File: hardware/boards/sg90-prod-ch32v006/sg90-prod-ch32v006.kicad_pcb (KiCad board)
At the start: 6 copper layers, 12.5 x 10 mm, 36 parts, among them J1 Servo Input, J2 Motor, J3 Debug, J4 Potentiometer, Q1 AO3401A, U1 TPAP2210K-3.3TRG1, U2 SN74LVC1G07DRLR_C19829624, U3 DRV8837DSGR-JSM, U4 CH32V006F8U6

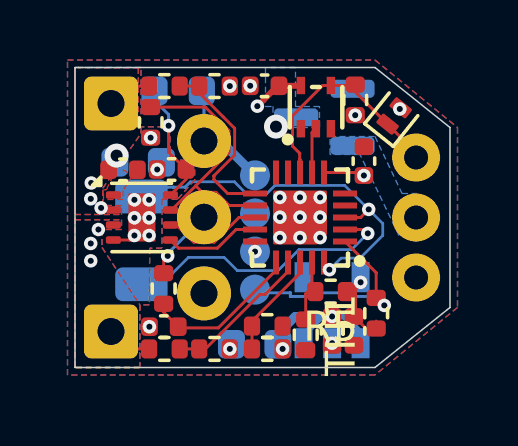
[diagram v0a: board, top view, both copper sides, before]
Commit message: make sg90-pprod-ch32v006 board DATA line 5v tolerant
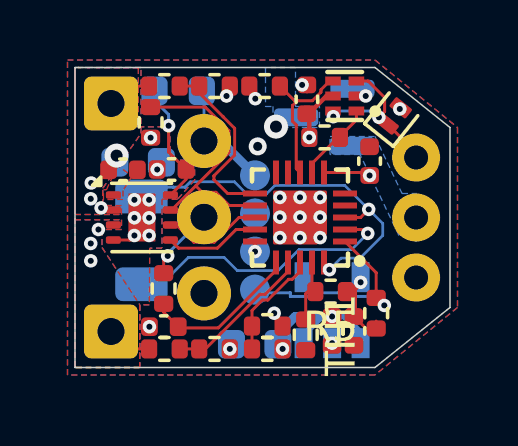
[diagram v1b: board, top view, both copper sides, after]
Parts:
- removed NT1: NetTie_2, shared:NetTie-2_SMD_0.2mm
- added R13: 47kΩ, Resistor_SMD:R_0402_1005Metric, F.Cu at (108.3, 92.3)
- D1: value PESD5V0L1UL -> ESD
- R1: value 1kΩ -> 10kΩ
- U2: value SN74LVC1G07DRLR_C19829624 -> SN74LVC2G07DRYR(UMW); footprint shared:SOT-553-5_L1.6-W1.2-P0.50-LS1.6-BL -> shared:SON-6_L1.5-W1.0-P0.50-BL
- moved R1 3.05 mm to (106.3, 90.6), turned to 0 degrees
- moved C4 1.48 mm to (107.7, 91.1), turned to 90 degrees
- moved U2 1.03 mm to (109.0, 91.0), turned to 90 degrees
- moved C9 0.19 mm to (109.8, 93.1)
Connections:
- R1 pad 2: /DATA -> /RX
- U2 pad 1: unconnected-(U2-NC-Pad1) -> /TX
- U2 pad 2: /TX -> GND
- U2 pad 3: GND -> /DATA
- U2 pad 4: /DATA -> /RX
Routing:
- net /RX: track 0.44 -> 4.85 mm
- net /DATA: track 7.19 -> 5.10 mm, vias 0 -> 2
- net /TX: track 1.51 -> 2.70 mm
- net GND: track 0.00 -> 0.25 mm, vias 15 -> 18

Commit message: echo-free data line with RX disable latch
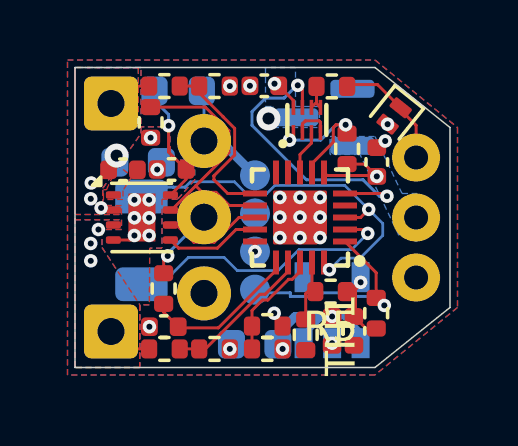
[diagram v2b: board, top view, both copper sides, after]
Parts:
- R1: value 10kΩ -> 47kΩ
- R13: value 47kΩ -> 68Ω
- U2: value SN74LVC2G07DRYR(UMW) -> 74LVC2G125; footprint shared:SON-6_L1.5-W1.0-P0.50-BL -> shared:X2-DFN1210-8_L1.2-W1.0-P0.30-BL
- moved R1 3.45 mm to (109.1, 92.7), turned to -90 degrees
- moved R13 1.72 mm to (108.6, 90.6), turned to 0 degrees
- moved U2 1.49 mm to (107.7, 91.8), turned to 0 degrees
- moved C4 1.49 mm to (106.3, 90.6), turned to 180 degrees
- moved C9 0.24 mm to (110.1, 93.2)
- turned D1 to -128.659 degrees
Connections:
- R1 pad 1: +3.3V -> /TX
- R1 pad 2: /RX -> +3.3V
- R13 pad 1: /TX -> /BUF
- R13 pad 2: +3.3V -> /DATA
- U2 pad 3: /DATA -> /RX
- U2 pad 4: /RX -> GND
- U2 pad 5: +3.3V -> /BUF
- U2 pad 6: /DATA -> /BUF
- U4 pad 5: unconnected-(U4-PD0/T1/TX_/SDA_/OPN1-Pad5) -> /DE
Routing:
- net /DE: track 0.00 -> 10.1 mm, vias 0 -> 2
- net /RX: track 4.85 -> 1.49 mm
- net /BUF: track 0.00 -> 1.52 mm
- net /TX: track 2.70 -> 4.02 mm, vias 0 -> 2
- net /DATA: track 5.10 -> 3.95 mm, vias 2 -> 0
- net GND: track 0.25 -> 1.30 mm, vias 18 -> 17
- net /OUTB: track 1.51 -> 0.69 mm
- net /OUTA: track 1.51 -> 0.69 mm
- net /VSYS: track 5.45 -> 4.77 mm
- net +3.3V: track 9.87 -> 9.31 mm, vias 4 -> 3
- net /VSNB: track 4.98 -> 4.47 mm

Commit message: Normalize line endings to LF
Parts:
- removed NT3: NetTie_2, shared:NetTie-2_SMD_0.2mm
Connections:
- net /ISNS+ renamed /ISNS
- U4 pad 2: /ISNS- -> unconnected-(U4-PA1/T1/T2/OPN0/XI/A1-Pad2)
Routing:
- net /ISNS-: track 8.24 -> 0.00 mm, vias 1 -> 0
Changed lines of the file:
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@@
 	(net 8 "/OUTA")
 	(net 9 "/RX")
-	(net 10 "/ISNS+")
+	(net 10 "/ISNS")
 	(net 11 "/TX")
 	(net 12 "/DATA")
@@
 	(net 17 "/EN")
 	(net 18 "/VSNA")
-	(net 19 "/ISNS-")
+	(net 19 "unconnected-(U4-PA1{slash}T1{slash}T2{slash}OPN0{slash}XI{slash}A1-Pad2)")
 	(net 20 "+3.3V")
 	(net 21 "/VNTC")
@@
 			(size 0.2 0.8)
 			(layers "F.Cu" "F.Mask" "F.Paste")
-			(net 19 "/ISNS-")
+			(net 19 "unconnected-(U4-PA1{slash}T1{slash}T2{slash}OPN0{slash}XI{slash}A1-Pad2)")
 			(pinfunction "PA1/T1/T2/OPN0/XI/A1")
-			(pintype "bidirectional")
+			(pintype "bidirectional+no_connect")
 		)
 		(pad "3" smd rect
@@
 			(size 0.2 0.8)
 			(layers "F.Cu" "F.Mask" "F.Paste")
-			(net 10 "/ISNS+")
+			(net 10 "/ISNS")
 			(pinfunction "PA2/T1/T2/U2TX_/OPP0/XO/A0")
 			(pintype "bidirectional")
@@
 			(size 0.2 0.8)
 			(layers "F.Cu" "F.Mask" "F.Paste")
-			(net 10 "/ISNS+")
+			(net 10 "/ISNS")
 			(pinfunction "PD6/T2/RX/TX_/MOSI_/A6")
 			(pintype "bidirectional")
@@
 			(size 0.1 0.1)
 			(layers "B.Cu")
-			(net 10 "/ISNS+")
+			(net 10 "/ISNS")
 			(pinfunction "1")
 			(pintype "passive")
@@
 		)
 	)
-	(footprint "shared:NetTie-2_SMD_0.2mm"
-		(layer "B.Cu")
-		(at 103.15 96.86 180)
-		(descr "Net tie, 2 pin, 0.2mm trace width for fine pitch boards")
-		(tags "net tie")
-		(property "Reference" "NT3"
-			(at 0 0.7 0)
-			(layer "B.SilkS")
-			(hide yes)
-			(effects
-				(font
-					(size 0.5 0.5)
-					(thickness 0.1)
-				)
-				(justify mirror)
-			)
-		)
-		(property "Value" "NetTie_2"
-			(at 0 -0.7 0)
-			(layer "B.Fab")
-			(hide yes)
-			(effects
-				(font
-					(size 0.5 0.5)
-					(thickness 0.1)
-				)
-				(justify mirror)
-			)
-		)
-		(property "Datasheet" "~"
-			(at 0 0 0)
-			(layer "B.Fab")
-			(hide yes)
-			(effects
-				(font
-					(size 1.27 1.27)
-					(thickness 0.15)
-				)
-				(justify mirror)
-			)
-		)
-		(property "Description" "Net tie, 2 pins"
-			(at 0 0 0)
-			(layer "B.Fab")
-			(hide yes)
-			(effects
-				(font
-					(size 1.27 1.27)
-					(thickness 0.15)
-				)
-				(justify mirror)
-			)
-		)
-		(property ki_fp_filters "Net*Tie*")
-		(sheetname "/")
-		(sheetfile "sg90-prod-ch32v006.kicad_sch")
-		(attr exclude_from_pos_files exclude_from_bom allow_soldermask_bridges)
-		(net_tie_pad_groups "1,2")
-		(fp_line
-			(start 0.1 0)
-			(end -0.1 0)
-			(stroke
-				(width 0.1)
-				(type solid)
-			)
-			(layer "B.Cu")
-		)
-		(pad "1" smd circle
-			(at -0.1 0 180)
-			(size 0.1 0.1)
-			(layers "B.Cu")
-			(net 19 "/ISNS-")
-			(pinfunction "1")
-			(pintype "passive")
-			(clearance 0.1)
-		)
-		(pad "2" smd circle
-			(at 0.1 0 180)
-			(size 0.1 0.1)
-			(layers "B.Cu")
-			(net 1 "GND")
-			(pinfunction "2")
-			(pintype "passive")
-			(clearance 0.1)
-		)
-		(embedded_fonts no)
-	)
 	(footprint "Capacitor_SMD:C_0603_1608Metric"
 		(layer "B.Cu")
@@
 	)
 	(segment
-		(start 109.63 95.4)
-		(end 109.76 95.53)
-		(width 0.1)
-		(layer "F.Cu")
-		(net 19)
-	)
-	(segment
-		(start 109 95.4)
-		(end 109.63 95.4)
-		(width 0.1)
-		(layer "F.Cu")
-		(net 19)
-	)
-	(via
-		(at 109.76 95.53)
-		(size 0.45)
-		(drill 0.2)
-		(layers "F.Cu" "B.Cu")
-		(free yes)
-		(net 19)
-	)
-	(segment
-		(start 103.78 96.33)
-		(end 104.97 96.33)
-		(width 0.09)
-		(layer "B.Cu")
-		(net 19)
-	)
-	(segment
-		(start 104.97 96.33)
-		(end 105.41 96.77)
-		(width 0.09)
-		(layer "B.Cu")
-		(net 19)
-	)
-	(segment
-		(start 107.468 96.07)
-		(end 109.22 96.07)
-		(width 0.09)
-		(layer "B.Cu")
-		(net 19)
-	)
-	(segment
-		(start 103.25 96.86)
-		(end 103.78 96.33)
-		(width 0.09)
-		(layer "B.Cu")
-		(net 19)
-	)
-	(segment
-		(start 106.768 96.77)
-		(end 107.468 96.07)
-		(width 0.09)
-		(layer "B.Cu")
-		(net 19)
-	)
-	(segment
-		(start 109.22 96.07)
-		(end 109.76 95.53)
-		(width 0.09)
-		(layer "B.Cu")
-		(net 19)
-	)
-	(segment
-		(start 105.41 96.77)
-		(end 106.768 96.77)
-		(width 0.09)
-		(layer "B.Cu")
-		(net 19)
-	)
-	(segment

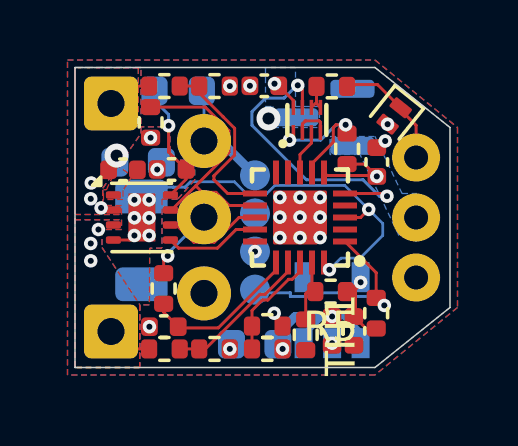
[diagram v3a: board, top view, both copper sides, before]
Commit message: add 0.1uF cap between motor terminals to reduce EMI
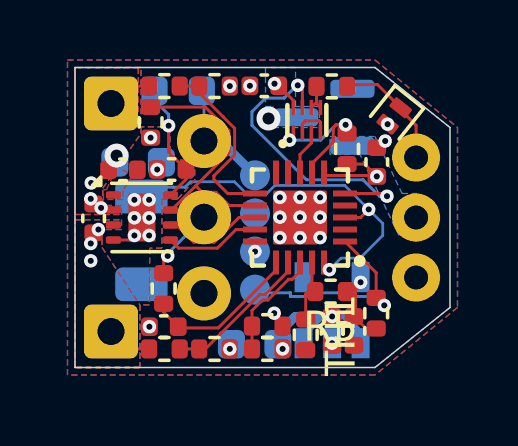
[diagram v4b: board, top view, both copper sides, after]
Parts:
- added C14: 0.1µF, Capacitor_SMD:C_0402_1005Metric, F.Cu at (100.6, 95.0)

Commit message: update sg90-prod-ch32v006
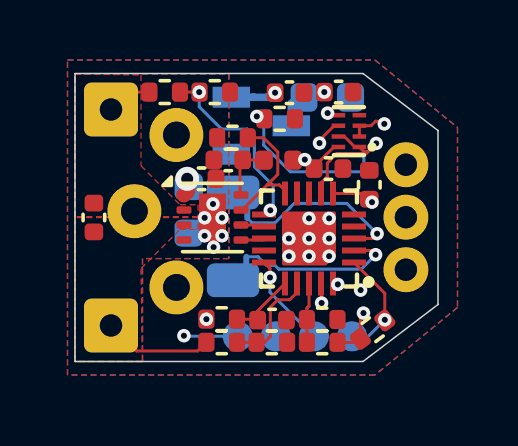
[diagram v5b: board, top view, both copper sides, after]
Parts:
- removed C14, C5: 0.1µF, Capacitor_SMD:C_0402_1005Metric
- removed D1: ESD, Diode_SMD:D_SOD-882
- removed Q1: AO3401A, Package_TO_SOT_SMD:SOT-23
- removed R10, R12: 10kΩ, Resistor_SMD:R_0402_1005Metric
- removed R11: 20kΩ, Resistor_SMD:R_0402_1005Metric
- removed R13: 68Ω, Resistor_SMD:R_0402_1005Metric
- removed U2: 74LVC2G125, shared:X2-DFN1210-8_L1.2-W1.0-P0.30-BL
- removed U3: DRV8837DSGR-JSM, Package_SON:WSON-8-1EP_2x2mm_P0.5mm_EP0.9x1.6mm
- added C10: 10µF, Capacitor_SMD:C_0603_1608Metric, B.Cu at (103.8, 94.7)
- added C11: 0.1µF, Capacitor_SMD:C_0402_1005Metric, F.Cu at (109.8, 93.9)
- added NT1: NetTie_2, shared:NetTie-2_SMD_0.2mm, B.Cu at (105.7, 94.8)
- added RS1: 0.1Ω 1%, Resistor_SMD:R_1206_3216Metric, B.Cu at (105.3, 95.6)
- added U5: CH32V006F8U6, shared:UQFN-20_L3.0-W3.0-P0.40-BL-EP1.7, F.Cu at (107.8, 95.7)
- added U6: 74LVC2G241GS,115, shared:XSON-8_L1.4-W1.0-P0.35-S0.55-BL, F.Cu at (109.1, 92.1)
- C3: value 1µF -> 10µF
- C8: value 10µF -> 0.1µF; footprint Capacitor_SMD:C_0603_1608Metric -> Capacitor_SMD:C_0402_1005Metric; moved to F.Cu
- FB1: footprint Inductor_SMD:L_0603_1608Metric -> Inductor_SMD:L_0402_1005Metric; moved to F.Cu
- R1: value 47kΩ -> 10kΩ
- R4: value 0.1Ω 1% -> 10kΩ; footprint Resistor_SMD:R_1206_3216Metric -> Resistor_SMD:R_0402_1005Metric; moved to F.Cu
- R5: value 10kΩ -> 20kΩ
- R9: value 20kΩ -> 10kΩ
- U1: value TPAP2210K-3.3TRG1 -> H7133-1; footprint shared:SOT-23-5_L2.9-W1.6-P0.95-LS2.8-BR -> shared:SOT-23-3_L2.9-W1.3-P1.90-LS2.4-BR
- U4: value CH32V006F8U6 -> DRV8837; footprint shared:UQFN-20_L3.0-W3.0-P0.40-BL-EP1.7 -> Package_SON:WSON-8-1EP_2x2mm_P0.5mm_EP0.9x1.6mm
- moved R9 10.0 mm to (108.2, 99.2), turned to 180 degrees
- moved R6 9.12 mm to (104.7, 90.8), turned to 0 degrees
- moved R5 8.65 mm to (103.0, 90.8), turned to 0 degrees
- moved C1 8.57 mm to (108.4, 91.0), turned to 0 degrees
- moved R4 8.26 mm to (109.9, 98.7), turned to 37.2 degrees
- moved C3 8.23 mm to (107.2, 90.8), turned to 0 degrees
- moved C2 7.96 mm to (108.8, 90.8), turned to 0 degrees
- moved U1 6.59 mm to (106.2, 91.9), turned to 180 degrees
- moved C6 6.04 mm to (106.6, 98.4), turned to 0 degrees
- moved C9 5.87 mm to (104.2, 93.7), turned to 0 degrees
- moved FB1 4.07 mm to (106.8, 93.1)
- moved J3 3.71 mm to (107.3, 99.0), turned to 0 degrees
- moved NT2 3.58 mm to (105.7, 96.5), turned to -90 degrees
- moved C7 3.53 mm to (105.1, 93.1), turned to 180 degrees
- moved C4 3.49 mm to (108.5, 93.4), turned to 0 degrees
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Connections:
- C1 pad 1: /VSYS -> VSYS
- C2 pad 1: /VSYS -> VSYS
- C3 pad 1: +3.3V -> +3V3
- C4 pad 1: +3.3V -> +3V3
- C6 pad 1: /3V3_DRV -> /VPOS
- C6 pad 2: PGND -> GND
- C7 pad 1: /VSYS -> /3V3_DRV
- C8 pad 1: /VSYS -> /MOT_A
- C8 pad 2: PGND -> /MOT_B
- C9 pad 1: +3.3V -> VSYS
- C9 pad 2: GND -> PGND
- FB1 pad 1: +3.3V -> +3V3
- J1 pad 1: GND -> VSYS
- J1 pad 2: VIN -> GND
- J2 pad 1: /OUTA -> /MOT_A
- J2 pad 2: /OUTB -> /MOT_B
- J3 pad 1: +3.3V -> +3V3
- J4 pad 1: +3.3V -> +3V3
- NT2 pad 1: /ISNS -> /ISNS-
- NT2 pad 2: PGND -> GND
- R1 pad 1: /TX -> GND
- R1 pad 2: +3.3V -> /TX_EN
- R4 pad 1: GND -> +3V3
- R4 pad 2: PGND -> /nRST
- R5 pad 1: +3.3V -> /MOT_A
- R5 pad 2: /VNTC -> /VSNA
- R6 pad 1: +3.3V -> /VSNA
- R6 pad 2: /nRST -> GND
- R7 pad 1: /VSYS -> /MOT_B
- R7 pad 2: /VINS -> /VSNB
- R8 pad 1: /VINS -> /VSNB
- R9 pad 1: /OUTA -> +3V3
- R9 pad 2: /VSNA -> /VNTC
- U1 pad 1: /VSYS -> GND
- U1 pad 2: GND -> +3V3
- U1 pad 3: /VSYS -> VSYS
- U4 pad 1: /nRST -> VSYS
- U4 pad 2: unconnected-(U4-PA1/T1/T2/OPN0/XI/A1-Pad2) -> /MOT_A
- U4 pad 3: /ISNS -> /MOT_B
- U4 pad 4: GND -> PGND
- U4 pad 5: /DE -> /IN2
- U4 pad 6: +3.3V -> /IN1
- U4 pad 7: /TX -> /EN
- U4 pad 8: /RX -> /3V3_DRV
- U4 pad 9: unconnected-(U4-PC2/T1C3N_/T2/SCL-Pad9) -> PGND
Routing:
- net VSYS: track 0.00 -> 15.1 mm, vias 0 -> 2
- net /ISNS: track 11.4 -> 0.00 mm, vias 2 -> 0
- net /TX_EN: track 0.00 -> 10.1 mm, vias 0 -> 2
- net /DE: track 10.1 -> 0.00 mm, vias 2 -> 0
- net +3.3V: track 9.31 -> 0.00 mm, vias 3 -> 0
- net +3V3: track 0.00 -> 8.57 mm, vias 0 -> 5
- net /RX: track 1.49 -> 7.85 mm, vias 0 -> 2
- net /ISNS+: track 0.00 -> 5.92 mm, vias 0 -> 1
- net /ISNS-: track 0.00 -> 5.46 mm, vias 0 -> 1
- net /VSYS: track 4.77 -> 0.00 mm, vias 4 -> 0
- net /EN: track 8.62 -> 4.43 mm
- net /DATA: track 3.95 -> 7.88 mm, vias 0 -> 1
- net /nRST: track 7.43 -> 3.68 mm
- net /MOT_B: track 0.00 -> 3.65 mm
- net /VINS: track 3.42 -> 0.00 mm
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- added copper zone on In1.Cu, net +3V3
- added copper zone on F.Cu, net /MOT_A
- added copper zone on F.Cu, net /MOT_B
- added copper zone on In2.Cu, net GND
- added copper zone on In2.Cu, net PGND
- removed copper zone on In2.Cu, net +3.3V
- removed copper zone on B.Cu, net /OUTA
- removed copper zone on F.Cu, net /OUTA
- removed copper zone on B.Cu, net /OUTB
- removed copper zone on F.Cu, net /OUTB
- removed copper zone on B.Cu, net /VSYS
- removed copper zone on F.Cu, net /VSYS
- removed copper zone on In4.Cu, net /VSYS
- removed copper zone on In1.Cu, net GND
- removed copper zone on In3.Cu, net GND
- removed copper zone on In4.Cu, net GND
- removed copper zone on In3.Cu, net PGND
- removed copper zone on B.Cu, net VIN
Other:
- board size 12.5 x 10 mm -> 12.1 x 9.6 mm
- copper layers 6 -> 4
- board text added: "+"
- board text added: "-"
- board text added: "A"
- board text added: "B"
- board text added: "D"
- board text added: "R S G V"
- board text added: "W"

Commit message: rebuilt board
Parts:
- removed C3: 10µF, Capacitor_SMD:C_0402_1005Metric
- C1: value 10µF -> 1µF; footprint Capacitor_SMD:C_0603_1608Metric -> Capacitor_SMD:C_0402_1005Metric; moved to F.Cu
- C2: value 1µF -> 4.7µF
- C4, C7, C8, C9, FB1, R3, U4, U6: moved to B.Cu
- J4: moved to F.Cu
- NT1, NT2: footprint shared:NetTie-2_SMD_0.2mm -> shared:NetTie-2_SMD_0.127mm
- RS1: value 0.1Ω 1% -> 10mΩ 1%; footprint Resistor_SMD:R_1206_3216Metric -> Resistor_SMD:R_0805_2012Metric
- U1: value H7133-1 -> TLV76733DRVR; footprint shared:SOT-23-3_L2.9-W1.3-P1.90-LS2.4-BR -> Package_SON:WSON-6-1EP_2x2mm_P0.65mm_EP1x1.6mm; moved to F.Cu
- moved R7 8.58 mm to (103.0, 90.8)
- moved R8 8.58 mm to (104.7, 90.8)
- moved R6 8.41 mm to (104.7, 99.2)
- moved R5 8.41 mm to (103.0, 99.2)
- moved C2 8.22 mm to (106.8, 98.8), turned to -90 degrees
- moved C1 7.79 mm to (110.3, 98.6), turned to 37.235 degrees
- moved U1 7.06 mm to (108.3, 98.7), turned to 0 degrees
- moved FB1 5.69 mm to (107.3, 98.8), turned to 90 degrees
- moved NT2 4.87 mm to (105.9, 91.6), turned to 180 degrees
- moved C7 3.76 mm to (106.6, 96.5)
- moved RS1 3.34 mm to (105.1, 92.3), turned to -90 degrees
- moved C10 3.30 mm to (105.7, 97.4), turned to 0 degrees
- moved C9 2.88 mm to (104.9, 96.5)
- moved J3 2.61 mm to (109.2, 97.1), turned to 90 degrees
- moved R9 2.30 mm to (106.0, 98.8), turned to 90 degrees
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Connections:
- C2 pad 1: VSYS -> +3V3
- U1 pad 1: GND -> +3V3
- U1 pad 3: VSYS -> GND
- U5 pad 10: /EN -> unconnected-(U5-PC3/T1C3/T2C3_4-Pad10)
- U5 pad 11: /VSNA -> /VSNB
- U5 pad 12: /IN1 -> /IN2
- U5 pad 13: /IN2 -> /IN1
- U5 pad 14: unconnected-(U5-PC7-Pad14) -> /EN
- U5 pad 17: /VSNB -> /VSNA
- U5 pad 19: /RX -> unconnected-(U5-PD5/A5-Pad19)
- U5 pad 20: /TX -> unconnected-(U5-PD6/A6-Pad20)
- U5 pad 7: /TX_EN -> /TX
- U5 pad 8: unconnected-(U5-PC1/RX_3-Pad8) -> /RX
- U5 pad 9: unconnected-(U5-PC2/T2C2_2-Pad9) -> /TX_EN
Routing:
- net VSYS: track 15.1 -> 0.65 mm
- net /RX: track 7.85 -> 1.80 mm, vias 2 -> 1
- net /TX: track 6.83 -> 1.82 mm, vias 2 -> 1
- net /TX_EN: track 10.1 -> 6.10 mm
- net /ISNS-: track 5.46 -> 8.28 mm, vias 1 -> 2
- net /DATA: track 7.88 -> 5.21 mm, vias 1 -> 0
- net /nRST: track 3.68 -> 1.42 mm
- net GND: track 0.00 -> 2.21 mm, vias 9 -> 13
- net +3V3: track 8.57 -> 6.53 mm, vias 5 -> 4
- net /MOT_B: track 3.65 -> 1.79 mm
- net /3V3_DRV: track 1.92 -> 3.47 mm
- net /VNTC: track 1.99 -> 3.48 mm
- net /VSNB: track 3.56 -> 5.01 mm
- net /POT: track 5.00 -> 3.66 mm, vias 1 -> 0
- net /EN: track 4.43 -> 3.38 mm, vias 0 -> 1
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- added copper zone on F.Cu, net +3V3
- added copper zone on In2.Cu, net +3V3
- added copper zone on B.Cu, net /MOT_A
- added copper zone on B.Cu, net /MOT_B
- added copper zone on In1.Cu, net GND
- added copper zone on B.Cu, net VSYS
- added copper zone on F.Cu, net VSYS
- added copper zone on In2.Cu, net VSYS
- removed copper zone on In1.Cu, net +3V3
- removed copper zone on F.Cu, net /MOT_A
- removed copper zone on F.Cu, net /MOT_B
- removed copper zone on In2.Cu, net GND
- removed copper zone on F.Cu, net PGND
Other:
- board text removed: "+"
- board text removed: "-"
- board text removed: "A"
- board text removed: "B"
- board text removed: "D"
- board text removed: "R S G V"
- board text removed: "W"
